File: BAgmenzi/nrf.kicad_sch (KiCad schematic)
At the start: 8 parts, among them J5 3220-10-0100-00

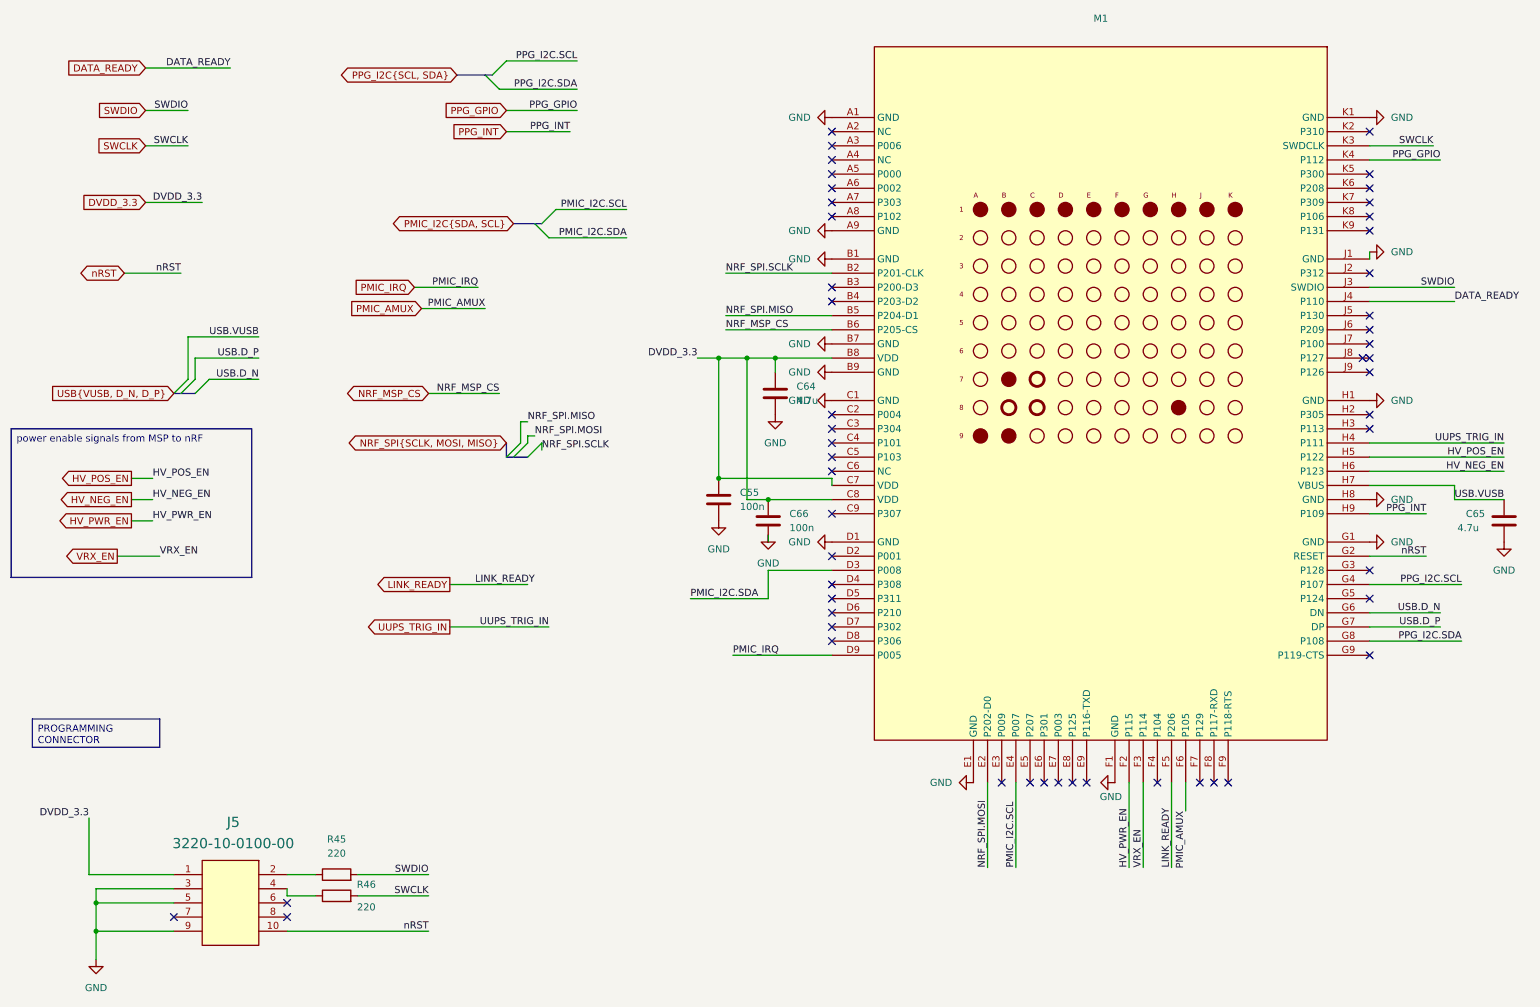
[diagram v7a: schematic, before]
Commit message: added polyCMUT footprint, changed enables, more compact
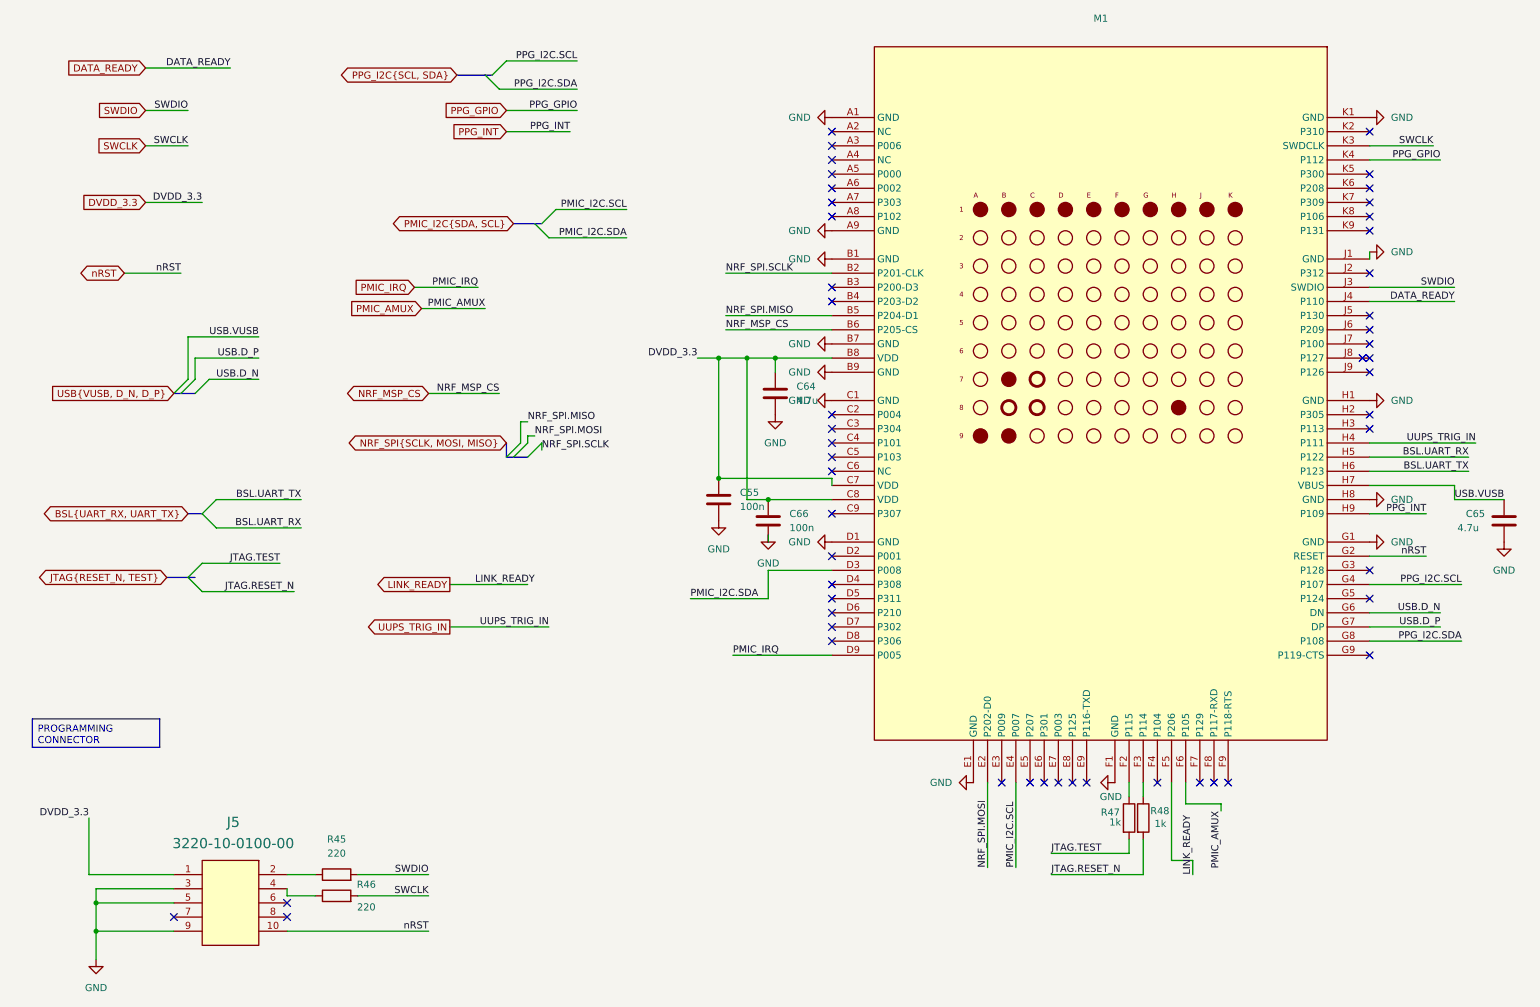
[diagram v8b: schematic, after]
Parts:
- added R47, R48: 1k, Resistor_SMD:R_0402_1005Metric, symbol Device:R
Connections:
- net HV_NEG_EN renamed BSL.UART_TX
- net HV_POS_EN renamed BSL.UART_RX
- net HV_PWR_EN: no longer names the net of M1.F2 (P115)
- net HV_PWR_EN: now also R47.1
- net VRX_EN: no longer names the net of M1.F3 (P114)
- net VRX_EN: now also R48.1
- new net JTAG.RESET_N: R48.2
- new net JTAG.TEST: R47.2
